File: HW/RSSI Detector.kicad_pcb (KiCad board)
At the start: 2 copper layers, 35.6 x 17.8 mm, 28 parts, among them P1 SMA, P2 SMA, U1 AD8319, U2 AD8319, U3 Teensy3.2, X1 CX3099NL

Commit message: layout finished
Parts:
- moved R1 3.70 mm to (169.2, 84.3), turned to 270 degrees
- moved C1 2.82 mm to (170.9, 84.3), turned to 270 degrees
- moved C3 1.32 mm to (156.7, 84.4), turned to 180 degrees
- moved C12 1.17 mm to (146.6, 87.4), turned to 180 degrees
- moved C13 1.15 mm to (167.4, 84.3), turned to 270 degrees
- moved C11 0.99 mm to (146.6, 85.9), turned to 180 degrees
- moved C2 0.82 mm to (156.7, 85.9), turned to 180 degrees
- moved C4 0.14 mm to (162.8, 83.8)
- moved R2 0.10 mm to (157.8, 82.9)
- turned R10 to 270 degrees
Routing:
- net +3V3: track 0.00 -> 23.0 mm, vias 0 -> 2
- net Net-(R10-Pad2): track 0.00 -> 21.0 mm, vias 0 -> 2
- net Net-(R1-Pad2): track 0.00 -> 14.3 mm, vias 0 -> 2
- net /RF_IN: track 0.00 -> 13.5 mm
- net /RF_OUT: track 0.00 -> 13.1 mm
- net Net-(R5-Pad1): track 0.00 -> 4.91 mm
- net /ADC_A: track 0.00 -> 4.08 mm
- net /ADC_B: track 0.00 -> 3.95 mm
- net /A: track 0.00 -> 2.71 mm
- net /B: track 0.00 -> 2.68 mm
- net Net-(C10-Pad2): track 0.00 -> 2.31 mm
- net Net-(R8-Pad1): track 0.00 -> 2.03 mm
- net Net-(R7-Pad1): track 0.00 -> 1.96 mm
- net Net-(C5-Pad2): track 0.00 -> 1.77 mm
- net Net-(C4-Pad2): track 0.00 -> 1.75 mm
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- added copper zone on B.Cu, net GND
- added copper zone on F.Cu, net GND
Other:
- net class RF added: clearance 0.2, trace_width 0.82, via_dia 0.6, via_drill 0.4
- board text added: "RSSI Detector v1.0 Per0, 2017"
- board text added: "www.helentronica.com"

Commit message: 3d models finished
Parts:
- added P1: SMA, CONSMA003.062, F.Cu at (0.00, 0.00)
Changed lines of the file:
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@@
     (tracks 96)
     (zones 0)
-    (modules 28)
+    (modules 29)
     (nets 21)
   )
@@
     (pad_to_mask_clearance 0.2)
     (aux_axis_origin 0 0)
+    (grid_origin 138.43 97.79)
     (visible_elements FFFE7F7F)
     (pcbplotparams
@@
     (add_net /RF_OUT)
   )
+  (module CONSMA003.062 (layer F.Cu)
+    (at 0 0)
+    (fp_text reference P1 (at 0 7.62) (layer F.SilkS)
+      (effects (font (size 1.5 1.5) (thickness 0.15)))
+    )
+    (fp_text value SMA (at 0 -7.62) (layer F.SilkS) hide
+      (effects (font (size 1.5 1.5) (thickness 0.15)))
+    )
+    (fp_line (start 2.25 4.5) (end 2.25 -4.5) (layer Dwgs.User) (width 0.15))
+    (fp_line (start 2.25 -4.5) (end 12.25 -4.5) (layer Dwgs.User) (width 0.15))
+    (fp_line (start 12.25 -4.5) (end 12.25 4.5) (layer Dwgs.User) (width 0.15))
+    (fp_line (start 12.25 4.5) (end 2.25 4.5) (layer Dwgs.User) (width 0.15))
+    (pad 1 smd rect (at 0 0) (size 4.06 1.52) (layers F.Cu F.Paste F.Mask))
+    (pad 2 smd rect (at 0 -2.54) (size 4.06 1.52) (layers F.Cu F.Paste F.Mask)
+      (zone_connect 2) (thermal_width 4) (thermal_gap 0.3))
+    (pad 2 smd rect (at 0 2.54) (size 4.06 1.52) (layers F.Cu F.Paste F.Mask)
+      (zone_connect 2) (thermal_width 4) (thermal_gap 0.3))
+    (pad 2 smd rect (at 0 -2.54) (size 4.06 1.52) (layers B.Cu)
+      (zone_connect 2) (thermal_width 4) (thermal_gap 0.3))
+    (pad 2 smd rect (at 0 2.54) (size 4.06 1.52) (layers B.Cu)
+      (zone_connect 2) (thermal_width 4) (thermal_gap 0.3))
+    (pad 2 thru_hole circle (at 1.75 -2.1) (size 0.5 0.5) (drill 0.25) (layers *.Cu *.Mask F.SilkS)
+      (zone_connect 2))
+    (pad 2 thru_hole circle (at 1.25 -2.1) (size 0.5 0.5) (drill 0.25) (layers *.Cu *.Mask F.SilkS)
+      (zone_connect 2))
+    (pad 2 thru_hole circle (at 0.75 -2.1) (size 0.5 0.5) (drill 0.25) (layers *.Cu *.Mask F.SilkS)
+      (zone_connect 2))
+    (pad 2 thru_hole circle (at 0.25 -2.1) (size 0.5 0.5) (drill 0.25) (layers *.Cu *.Mask F.SilkS)
+      (zone_connect 2))
+    (pad 2 thru_hole circle (at -0.25 -2.1) (size 0.5 0.5) (drill 0.25) (layers *.Cu *.Mask F.SilkS)
+      (zone_connect 2))
+    (pad 2 thru_hole circle (at -0.75 -2.1) (size 0.5 0.5) (drill 0.25) (layers *.Cu *.Mask F.SilkS)
+      (zone_connect 2))
+    (pad 2 thru_hole circle (at -1.25 -2.1) (size 0.5 0.5) (drill 0.25) (layers *.Cu *.Mask F.SilkS)
+      (zone_connect 2))
+    (pad 2 thru_hole circle (at -1.75 -2.1) (size 0.5 0.5) (drill 0.25) (layers *.Cu *.Mask F.SilkS)
+      (zone_connect 2))
+    (pad 2 thru_hole circle (at 1.75 2.1) (size 0.5 0.5) (drill 0.25) (layers *.Cu *.Mask F.SilkS)
+      (zone_connect 2))
+    (pad 2 thru_hole circle (at 1.25 2.1) (size 0.5 0.5) (drill 0.25) (layers *.Cu *.Mask F.SilkS)
+      (zone_connect 2))
+    (pad 2 thru_hole circle (at 0.75 2.1) (size 0.5 0.5) (drill 0.25) (layers *.Cu *.Mask F.SilkS)
+      (zone_connect 2))
+    (pad 2 thru_hole circle (at 0.25 2.1) (size 0.5 0.5) (drill 0.25) (layers *.Cu *.Mask F.SilkS)
+      (zone_connect 2))
+    (pad 2 thru_hole circle (at -0.25 2.1) (size 0.5 0.5) (drill 0.25) (layers *.Cu *.Mask F.SilkS)
+      (zone_connect 2))
+    (pad 2 thru_hole circle (at -0.75 2.1) (size 0.5 0.5) (drill 0.25) (layers *.Cu *.Mask F.SilkS)
+      (zone_connect 2))
+    (pad 2 thru_hole circle (at -1.25 2.1) (size 0.5 0.5) (drill 0.25) (layers *.Cu *.Mask F.SilkS)
+      (zone_connect 2))
+    (pad 2 thru_hole circle (at -1.75 2.1) (size 0.5 0.5) (drill 0.25) (layers *.Cu *.Mask F.SilkS)
+      (zone_connect 2))
+    (model "D:/Elektronika/Microwavino Detector/HW/3d/User Library-RP_SMA_PCB-1.wrl"
+      (at (xyz 0.08 0 0.005))
+      (scale (xyz 200 200 200))
+      (rotate (xyz 0 180 90))
+    )
+  )
   (module vna:C_0603b (layer F.Cu)

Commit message: put Henrik's coupler
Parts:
- removed the P1 at (0.00, 0.00)
- removed X1: CX3099NL, vna:CX3099NL
- added F1: COUPLER, vna:coupler4, F.Cu at (155.4, 90.9)
- added R11: 49.9, vna:R_0402b, F.Cu at (154.7, 87.9)
- added R12: 49.9, vna:R_0402b, F.Cu at (156.5, 87.9)
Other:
- copper layers 2 -> 4

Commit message: layout done
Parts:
- moved P2 31.0 mm to (171.7, 92.3), turned to 0 degrees
- moved P1 31.0 mm to (140.7, 92.1), turned to 180 degrees
- moved C2 12.6 mm to (144.1, 85.8)
- moved C3 12.6 mm to (144.1, 84.3)
- moved R3 12.2 mm to (148.2, 82.8)
- moved R2 12.2 mm to (145.6, 82.8)
- moved R5 12.2 mm to (143.1, 82.9)
- moved C4 12.2 mm to (150.6, 83.8)
- moved U1 12.1 mm to (148.1, 85.0)
- moved C6 12.0 mm to (145.8, 87.1)
- moved R4 11.8 mm to (148.2, 88.4)
- moved C5 11.8 mm to (148.3, 87.1)
- moved C8 11.8 mm to (163.6, 87.4)
- moved R6 11.8 mm to (163.7, 88.6)
- moved U2 11.8 mm to (161.8, 85.2)
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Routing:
- net Net-(R1-Pad2): track 14.3 -> 26.4 mm
- net Net-(R10-Pad2): track 21.0 -> 9.30 mm
- net /RF_IN: track 13.5 -> 6.27 mm
- net /RF_OUT: track 13.1 -> 6.83 mm
- net Net-(R7-Pad1): track 1.96 -> 4.84 mm
- net +3V3: track 23.0 -> 25.4 mm
- net Net-(R3-Pad1): track 1.66 -> 0.00 mm
- net /A: track 2.71 -> 1.28 mm
- net Net-(C10-Pad2): track 2.31 -> 1.33 mm
- net Net-(F1-Pad5): track 0.00 -> 0.73 mm
- net Net-(F1-Pad4): track 0.00 -> 0.67 mm
- net Net-(R5-Pad1): track 4.91 -> 4.32 mm

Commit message: layout almost complete
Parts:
- added REF**: Via_0.3_0.6, vna:Via_0.3_0.6, F.Cu at (168.4, 93.7)
- added REF**: Via_0.3_0.6, vna:Via_0.3_0.6, F.Cu at (158.8, 87.1)
- added REF**: Via_0.3_0.6, vna:Via_0.3_0.6, F.Cu at (155.7, 83.6)
- added REF**: Via_0.3_0.6, vna:Via_0.3_0.6, F.Cu at (156.2, 86.1)
- added REF**: Via_0.3_0.6, vna:Via_0.3_0.6, F.Cu at (145.5, 87.6)
- added REF**: Via_0.3_0.6, vna:Via_0.3_0.6, F.Cu at (144.5, 87.1)
- added REF**: Via_0.3_0.6, vna:Via_0.3_0.6, F.Cu at (149.6, 89.2)
- added REF**: Via_0.3_0.6, vna:Via_0.3_0.6, F.Cu at (149.6, 88.1)
- added REF**: Via_0.3_0.6, vna:Via_0.3_0.6, F.Cu at (151.6, 83.6)
- added REF**: Via_0.3_0.6, vna:Via_0.3_0.6, F.Cu at (145.5, 82.5)
- added REF**: Via_0.3_0.6, vna:Via_0.3_0.6, F.Cu at (141.5, 83.1)
- added REF**: Via_0.3_0.6, vna:Via_0.3_0.6, F.Cu at (166.4, 93.7)
- added REF**: Via_0.3_0.6, vna:Via_0.3_0.6, F.Cu at (142.5, 84.1)
- added REF**: Via_0.3_0.6, vna:Via_0.3_0.6, F.Cu at (142.5, 85.6)
- added REF**: Via_0.3_0.6, vna:Via_0.3_0.6, F.Cu at (145.0, 93.7)
- added REF**: Via_0.3_0.6, vna:Via_0.3_0.6, F.Cu at (143.5, 93.7)
- added REF**: Via_0.3_0.6, vna:Via_0.3_0.6, F.Cu at (143.5, 90.7)
- added REF**: Via_0.3_0.6, vna:Via_0.3_0.6, F.Cu at (145.0, 90.7)
- added REF**: Via_0.3_0.6, vna:Via_0.3_0.6, F.Cu at (166.4, 90.7)
- added REF**: Via_0.3_0.6, vna:Via_0.3_0.6, F.Cu at (168.4, 90.7)
- added REF**: Via_0.3_0.6, vna:Via_0.3_0.6, F.Cu at (170.9, 86.1)
- added REF**: Via_0.3_0.6, vna:Via_0.3_0.6, F.Cu at (167.4, 86.1)
- added REF**: Via_0.3_0.6, vna:Via_0.3_0.6, F.Cu at (159.3, 82.5)
- added REF**: Via_0.3_0.6, vna:Via_0.3_0.6, F.Cu at (156.7, 84.1)
- added REF**: Via_0.3_0.6, vna:Via_0.3_0.6, F.Cu at (159.8, 88.1)
- moved OUT 0.14 mm to (171.7, 92.1)
- renumbered P1 to IN, P2 to OUT
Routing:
- net Net-(R3-Pad1): track 0.00 -> 1.51 mm
- net /A: track 1.28 -> 2.17 mm

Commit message: layout complete
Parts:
- added REF**: Via_0.3_0.6, vna:Via_0.3_0.6, F.Cu at (157.6, 87.5)
- added REF**: Via_0.3_0.6, vna:Via_0.3_0.6, F.Cu at (156.2, 95.6)
- added REF**: Via_0.3_0.6, vna:Via_0.3_0.6, F.Cu at (158.8, 95.6)
- added REF**: Via_0.3_0.6, vna:Via_0.3_0.6, F.Cu at (161.2, 95.6)
- added REF**: Via_0.3_0.6, vna:Via_0.3_0.6, F.Cu at (163.8, 95.6)
- added REF**: Via_0.3_0.6, vna:Via_0.3_0.6, F.Cu at (165.5, 94.6)
- added REF**: Via_0.3_0.6, vna:Via_0.3_0.6, F.Cu at (165.5, 93.9)
- added REF**: Via_0.3_0.6, vna:Via_0.3_0.6, F.Cu at (169.2, 92.8)
- added REF**: Via_0.3_0.6, vna:Via_0.3_0.6, F.Cu at (166.9, 92.8)
- added REF**: Via_0.3_0.6, vna:Via_0.3_0.6, F.Cu at (169.2, 91.4)
- added REF**: Via_0.3_0.6, vna:Via_0.3_0.6, F.Cu at (168.0, 91.4)
- added REF**: Via_0.3_0.6, vna:Via_0.3_0.6, F.Cu at (156.7, 87.1)
- added REF**: Via_0.3_0.6, vna:Via_0.3_0.6, F.Cu at (146.3, 94.7)
- added REF**: Via_0.3_0.6, vna:Via_0.3_0.6, F.Cu at (145.5, 91.4)
- added REF**: Via_0.3_0.6, vna:Via_0.3_0.6, F.Cu at (144.5, 92.8)
- added REF**: Via_0.3_0.6, vna:Via_0.3_0.6, F.Cu at (146.3, 93.9)
- added REF**: Via_0.3_0.6, vna:Via_0.3_0.6, F.Cu at (146.3, 90.3)
- added REF**: Via_0.3_0.6, vna:Via_0.3_0.6, F.Cu at (162.7, 88.5)
- added REF**: Via_0.3_0.6, vna:Via_0.3_0.6, F.Cu at (161.8, 88.5)
- added REF**: Via_0.3_0.6, vna:Via_0.3_0.6, F.Cu at (160.9, 88.5)
- added REF**: Via_0.3_0.6, vna:Via_0.3_0.6, F.Cu at (158.9, 88.5)
- added REF**: Via_0.3_0.6, vna:Via_0.3_0.6, F.Cu at (157.7, 88.5)
- added REF**: Via_0.3_0.6, vna:Via_0.3_0.6, F.Cu at (156.0, 87.1)
- added REF**: Via_0.3_0.6, vna:Via_0.3_0.6, F.Cu at (154.2, 88.5)
- added REF**: Via_0.3_0.6, vna:Via_0.3_0.6, F.Cu at (152.9, 88.5)
- added REF**: Via_0.3_0.6, vna:Via_0.3_0.6, F.Cu at (151.6, 88.5)
- added REF**: Via_0.3_0.6, vna:Via_0.3_0.6, F.Cu at (150.5, 88.5)
- added REF**: Via_0.3_0.6, vna:Via_0.3_0.6, F.Cu at (151.6, 83.6)
- added REF**: Via_0.3_0.6, vna:Via_0.3_0.6, F.Cu at (155.1, 87.1)
- added REF**: Via_0.3_0.6, vna:Via_0.3_0.6, F.Cu at (154.3, 87.5)
- added REF**: Via_0.3_0.6, vna:Via_0.3_0.6, F.Cu at (146.4, 95.5)
- added REF**: Via_0.3_0.6, vna:Via_0.3_0.6, F.Cu at (148.5, 95.5)
- added REF**: Via_0.3_0.6, vna:Via_0.3_0.6, F.Cu at (151.1, 95.6)
- added REF**: Via_0.3_0.6, vna:Via_0.3_0.6, F.Cu at (153.7, 95.6)
- moved REF** 1.70 mm to (166.9, 91.4)
- moved REF** 1.02 mm to (165.9, 92.8)
- moved REF** 1.02 mm to (145.5, 92.8)
- moved REF** 0.97 mm to (168.0, 92.8)
- moved REF** 0.92 mm to (165.9, 91.4)
- moved REF** 0.92 mm to (144.5, 91.4)
- moved REF** 0.89 mm to (143.5, 92.8)
- moved REF** 0.76 mm to (143.5, 91.4)
- moved REF** 0.40 mm to (159.9, 88.5)
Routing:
- added copper zone on In1.Cu, net GND
- added copper zone on In2.Cu, net GND
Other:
- net class RF: trace_width 0.82 -> 0.3

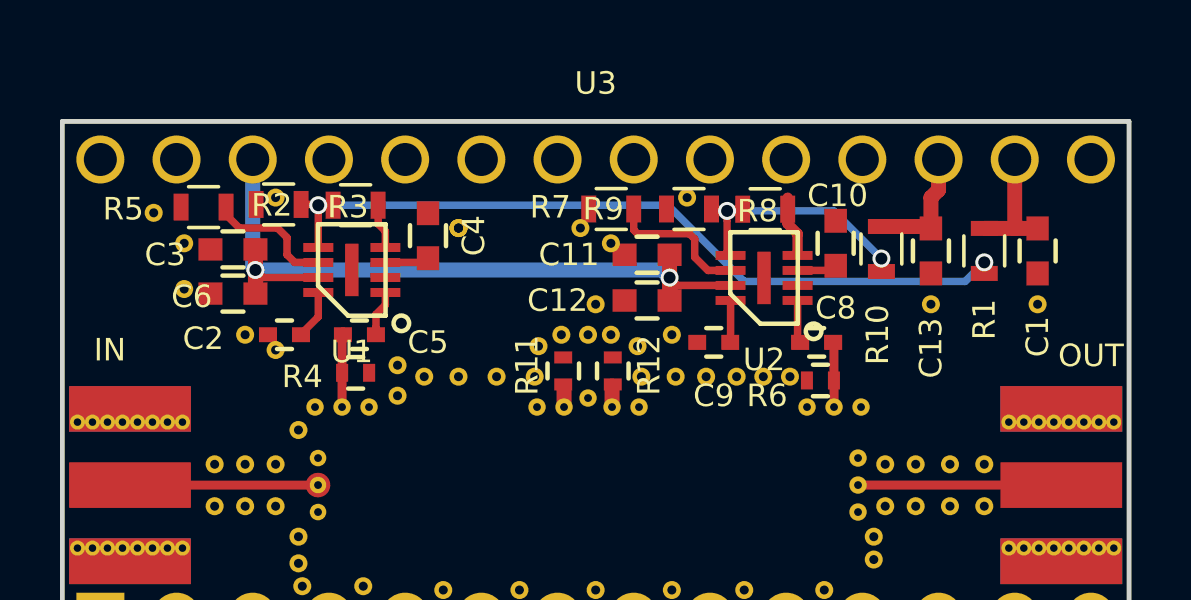
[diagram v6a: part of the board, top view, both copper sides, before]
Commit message: added temp adj transistor switch
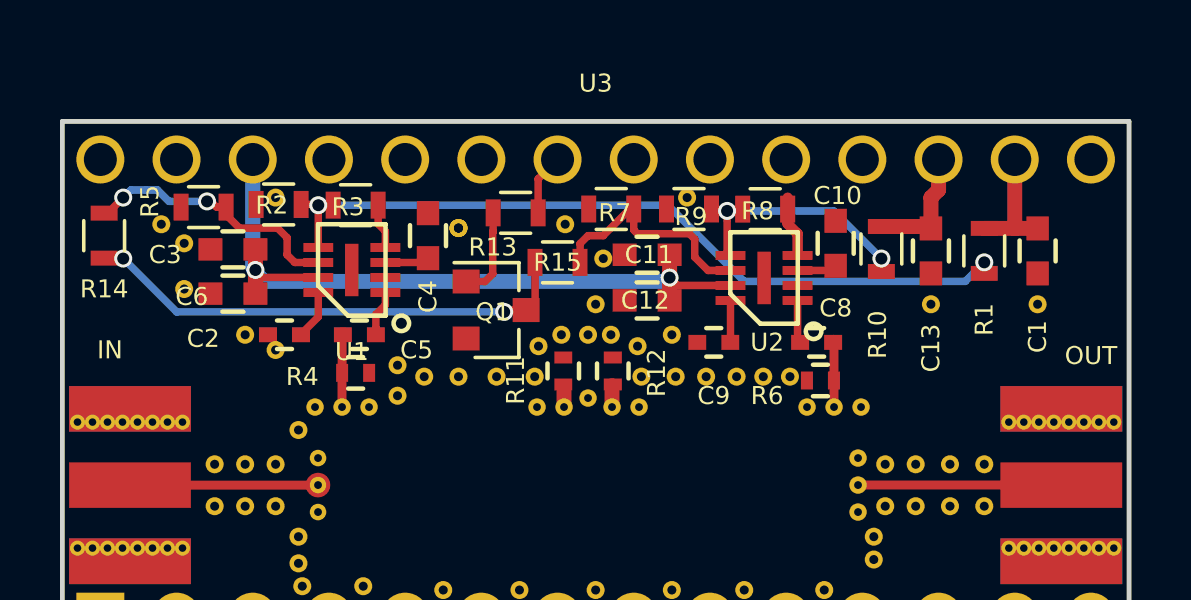
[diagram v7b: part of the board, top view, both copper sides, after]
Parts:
- added Q1: 2N7002P, TO_SOT_Packages_SMD:SOT-23, F.Cu at (152.9, 86.3)
- added R13: 1k, Resistors_SMD:R_0603, F.Cu at (153.5, 83.1)
- added R14: 510, Resistors_SMD:R_0603, F.Cu at (139.8, 83.8)
- added R15: 510, Resistors_SMD:R_0603, F.Cu at (154.9, 84.7)
- moved REF** 0.57 mm to (156.5, 84.6)
- moved REF** 0.52 mm to (155.2, 83.4)
- moved REF** 0.46 mm to (141.7, 83.4)
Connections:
- U3 pad 27: (no net) -> /TADJ_G
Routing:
- net Net-(Q1-Pad3): track 0.00 -> 16.5 mm, vias 0 -> 2
- net Net-(R14-Pad1): track 4.32 -> 8.94 mm, vias 0 -> 2
- net Net-(Q1-Pad1): track 0.00 -> 3.03 mm
- net Net-(R15-Pad1): track 4.84 -> 7.73 mm
- net /TADJ_G: track 0.00 -> 2.05 mm
